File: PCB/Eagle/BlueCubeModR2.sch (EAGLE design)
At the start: 33 parts, among them J3 2174507-2, U1 ESP32-PICO-D4, U2 CP2104-F03-GM, U4 STBC08, U7 NCP161

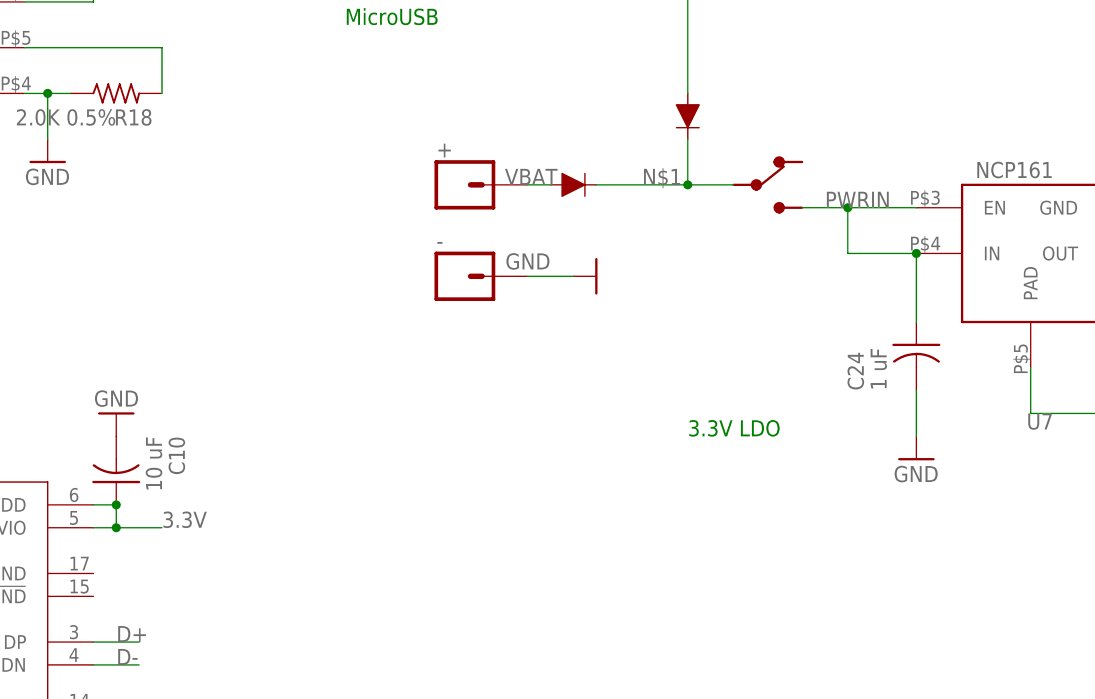
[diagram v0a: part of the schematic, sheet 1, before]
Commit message: Added v2 firmware w/ switch support
see updated readme for new build instructions
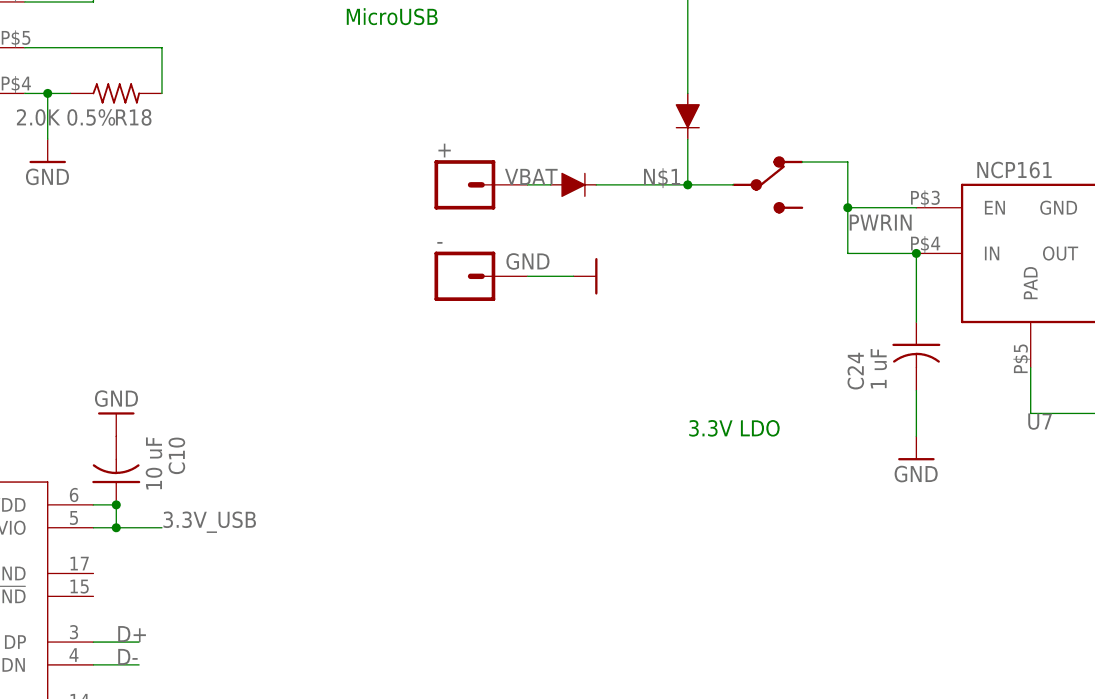
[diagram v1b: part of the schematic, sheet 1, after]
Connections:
- new net 3.3V_USB: C10.1, U2.VDD, U2.VIO
- net 3.3V: no longer C10.1, U2.VDD, U2.VIO
- net PWRIN: now also S2.1; no longer S2.3
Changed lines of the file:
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@@
 <wire x1="177.8" y1="88.9" x2="177.8" y2="96.52" width="0.1524" layer="91"/>
 <junction x="177.8" y="96.52"/>
-<label x="167.64" y="101.6" size="1.778" layer="95"/>
+<label x="170.18" y="99.06" size="1.778" layer="95"/>
 <pinref part="C24" gate="G$1" pin="1"/>
-<pinref part="S2" gate="G$1" pin="3"/>
-<wire x1="165.1" y1="101.6" x2="170.18" y2="101.6" width="0.1524" layer="91"/>
+<wire x1="170.18" y1="101.6" x2="170.18" y2="106.68" width="0.1524" layer="91"/>
 <junction x="170.18" y="101.6"/>
+<pinref part="S2" gate="G$1" pin="1"/>
+<wire x1="170.18" y1="106.68" x2="165.1" y2="106.68" width="0.1524" layer="91"/>
 </segment>
 </net>
@@
 <wire x1="203.2" y1="96.52" x2="220.98" y2="96.52" width="0.1524" layer="91"/>
 <junction x="220.98" y="104.14"/>
-</segment>
-<segment>
-<pinref part="U2" gate="IC" pin="VDD"/>
-<wire x1="88.9" y1="68.58" x2="86.36" y2="68.58" width="0.1524" layer="91"/>
-<pinref part="U2" gate="IC" pin="VIO"/>
-<wire x1="86.36" y1="66.04" x2="88.9" y2="66.04" width="0.1524" layer="91"/>
-<wire x1="88.9" y1="66.04" x2="88.9" y2="68.58" width="0.1524" layer="91"/>
-<label x="93.98" y="66.04" size="1.778" layer="95"/>
-<wire x1="88.9" y1="66.04" x2="93.98" y2="66.04" width="0.1524" layer="91"/>
-<junction x="88.9" y="66.04"/>
-<pinref part="C10" gate="G$1" pin="1"/>
-<junction x="88.9" y="68.58"/>
 </segment>
 </net>
@@
 </segment>
 </net>
+<net name="3.3V_USB" class="0">
+<segment>
+<pinref part="U2" gate="IC" pin="VDD"/>
+<wire x1="88.9" y1="68.58" x2="86.36" y2="68.58" width="0.1524" layer="91"/>
+<pinref part="U2" gate="IC" pin="VIO"/>
+<wire x1="86.36" y1="66.04" x2="88.9" y2="66.04" width="0.1524" layer="91"/>
+<wire x1="88.9" y1="66.04" x2="88.9" y2="68.58" width="0.1524" layer="91"/>
+<label x="93.98" y="66.04" size="1.778" layer="95"/>
+<wire x1="88.9" y1="66.04" x2="93.98" y2="66.04" width="0.1524" layer="91"/>
+<junction x="88.9" y="66.04"/>
+<pinref part="C10" gate="G$1" pin="1"/>
+<junction x="88.9" y="68.58"/>
+</segment>
+</net>
